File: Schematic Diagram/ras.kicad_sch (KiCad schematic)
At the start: 16 parts, among them Q1 S8050, SW2 SW_DPST_x2

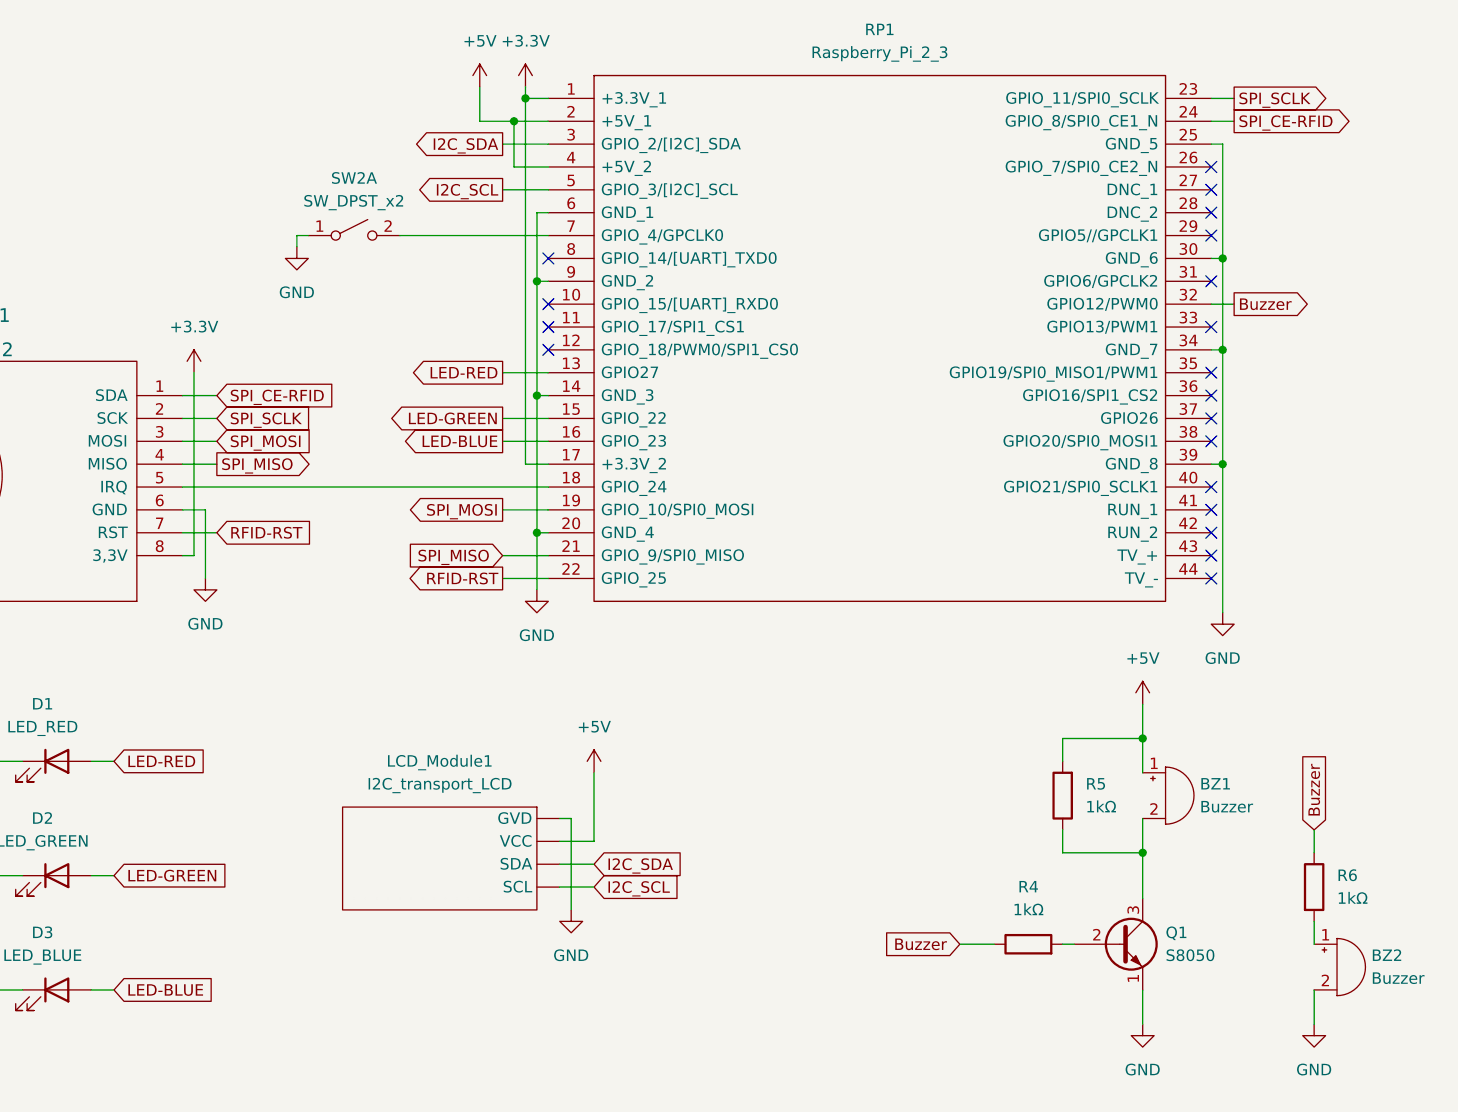
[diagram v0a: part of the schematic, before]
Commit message: update kicad before 9.0 after 8.0
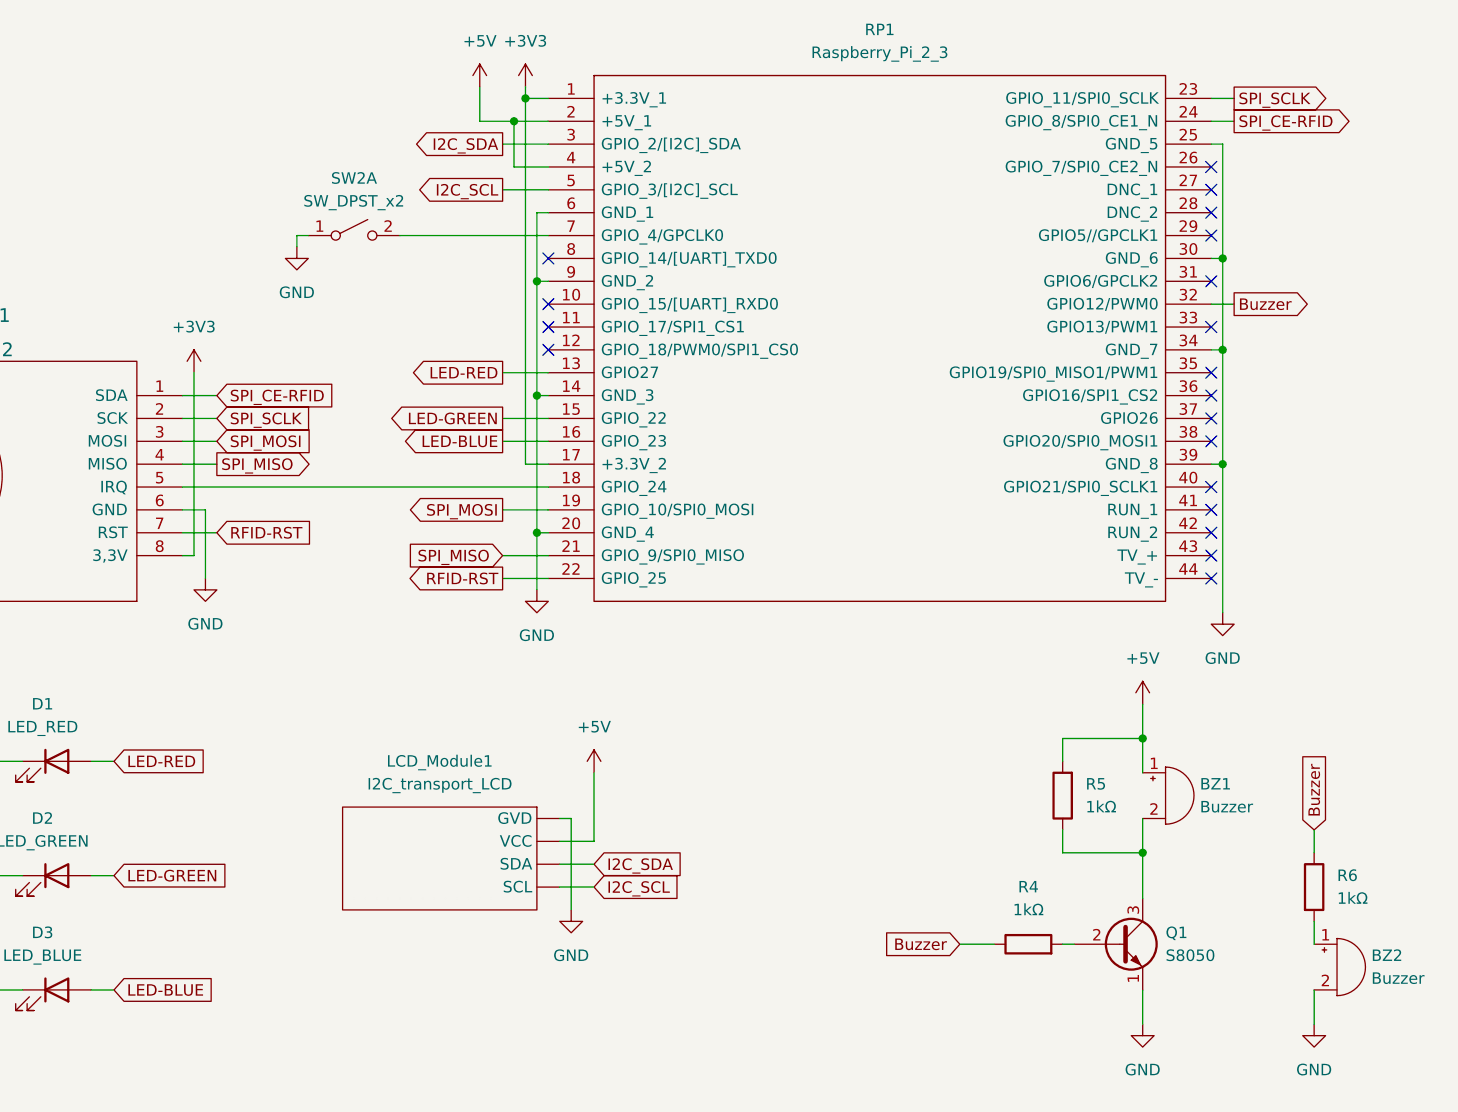
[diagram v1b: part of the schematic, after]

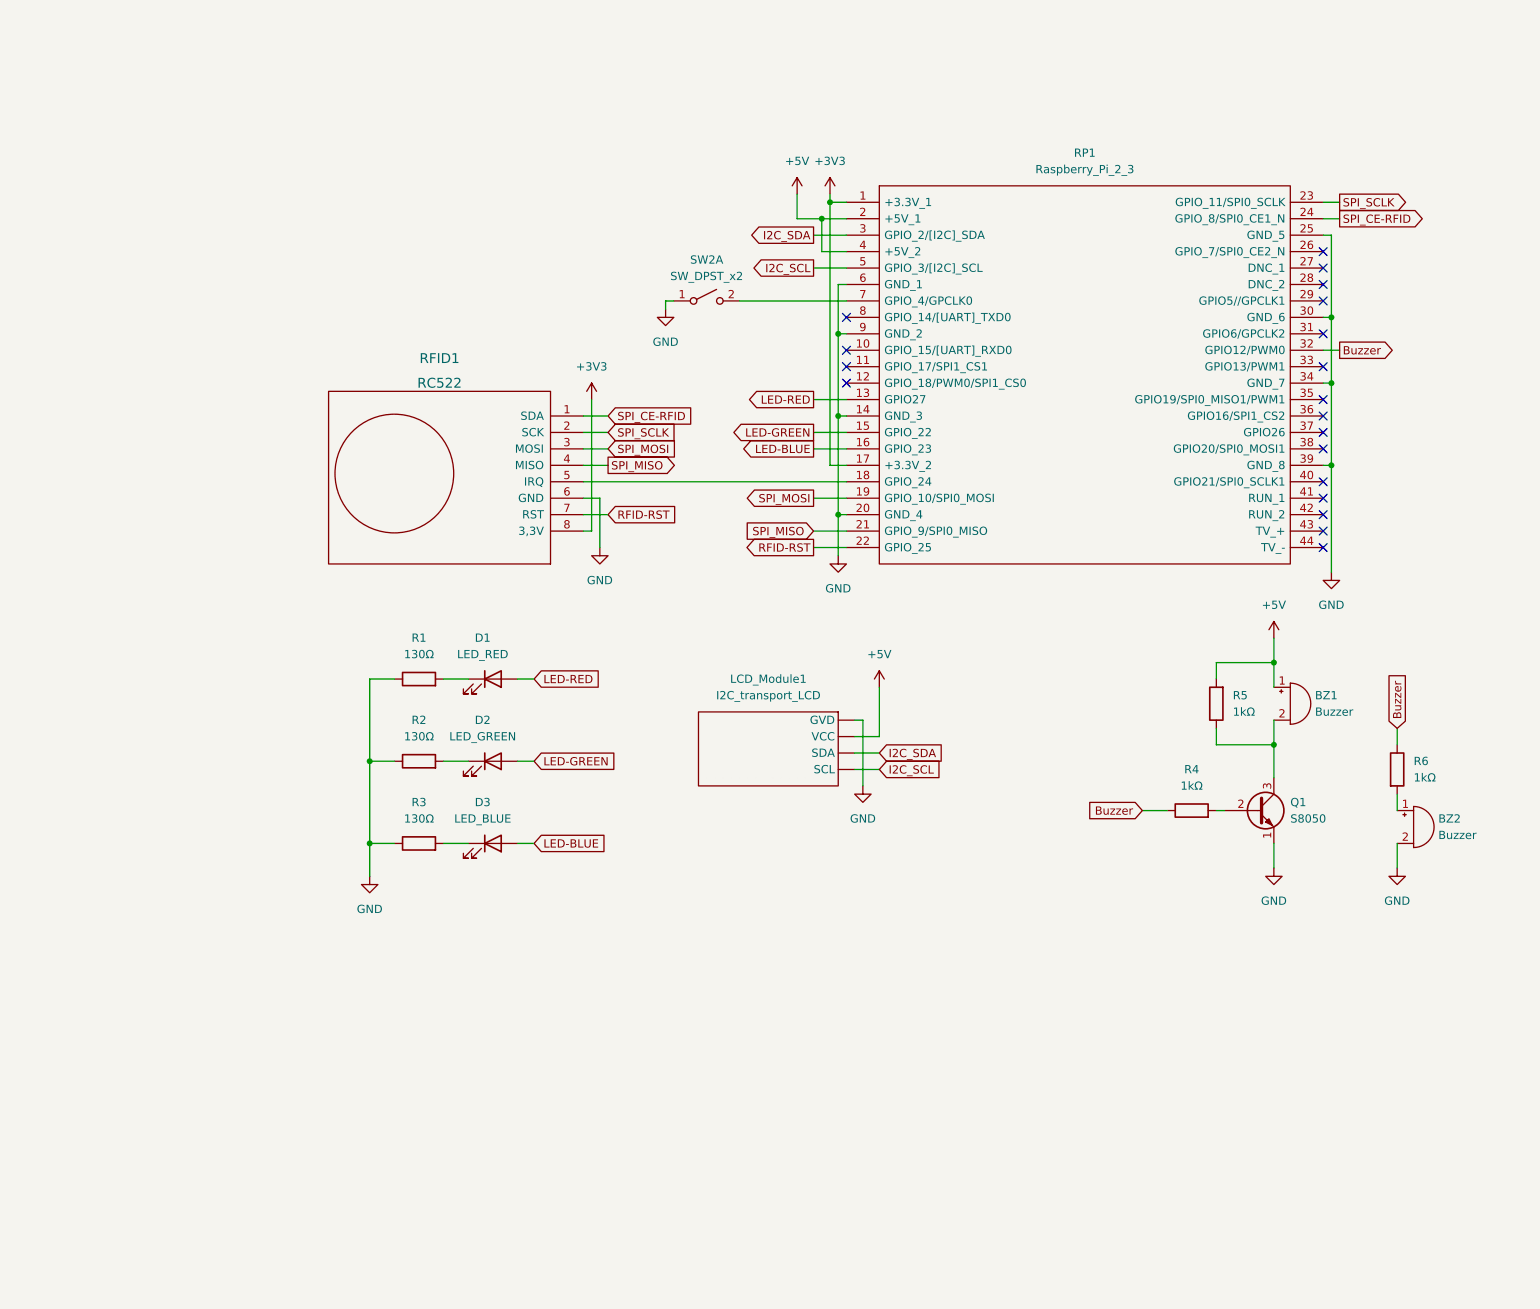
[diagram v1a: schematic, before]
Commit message: update ras and vertify RFID and LED
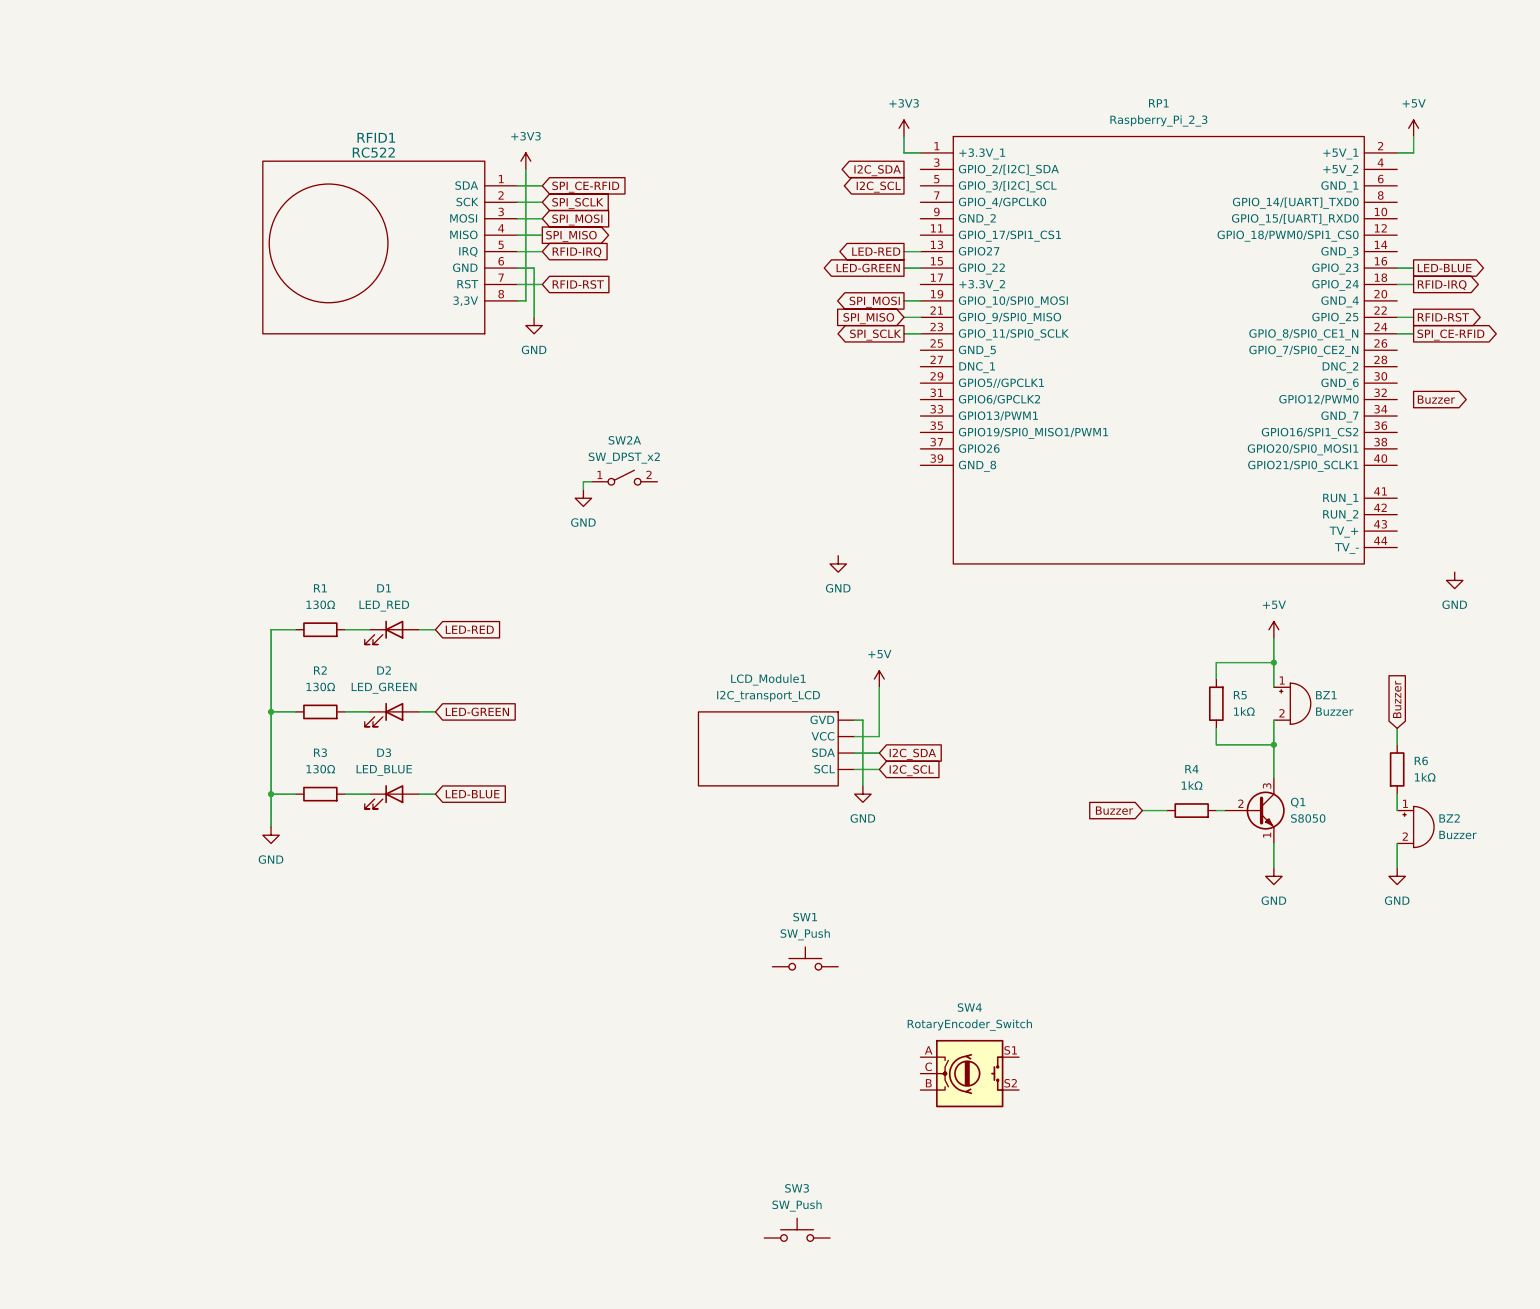
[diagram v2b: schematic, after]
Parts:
- added SW1, SW3: SW_Push, symbol Switch:SW_Push
- added SW4: RotaryEncoder_Switch, symbol Device:RotaryEncoder_Switch
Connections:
- net +3V3: no longer RP1.17 (+3.3V_2)
- net +5V: no longer RP1.4 (+5V_2)
- net Buzzer: no longer RP1.32 (GPIO12/PWM0)
- net GND: no longer RP1.14 (GND_3), RP1.20 (GND_4), RP1.25 (GND_5), RP1.30 (GND_6), RP1.34 (GND_7), RP1.39 (GND_8), RP1.6 (GND_1), RP1.9 (GND_2)
- net I2C_SCL: no longer RP1.5 (GPIO_3/[I2C]_SCL)
- net I2C_SDA: no longer RP1.3 (GPIO_2/[I2C]_SDA)
- net at SW2.2 (B): no longer RP1.7 (GPIO_4/GPCLK0)
- net RFID-IRQ: now reaches RFID1.5 (IRQ), RP1.18 (GPIO_24)
- no-connect marks 19 -> 0
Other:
- moved on the sheet: D1, D2, D3, R1, R2, R3, RFID1, RP1, SW2A

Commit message: verify I2C
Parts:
- added U2: ~, symbol project:AT24C32
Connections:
- net +5V: now also U2.5 (VCC)
- net GND: now also U2.6 (GND)
- net I2C_SCL: now also RP1.5 (GPIO_3/[I2C]_SCL), U2.3 (SCL)
- net I2C_SDA: now also RP1.3 (GPIO_2/[I2C]_SDA), U2.4 (SDA)
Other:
- moved on the sheet: LCD_Module1

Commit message: vertify encoder and button
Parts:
- removed SW2: SW_DPST_x2, symbol Switch:SW_DPST_x2
- removed SW3: SW_Push, symbol Switch:SW_Push
- added SW5, SW7, SW8, SW9: SW_Push, symbol Switch:SW_Push
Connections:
- net GND: now also SW1.1, SW4.C, SW4.S2, SW5.1, SW7.1, SW8.1, SW9.1
- net ENCODER_A: now reaches SW4.A
- net ENCODER_A: now also RP1.38 (GPIO20/SPI0_MOSI1)
- net ENCODER_B: now reaches SW4.B
- net ENCODER_B: now also RP1.40 (GPIO21/SPI0_SCLK1)
- net DONE_BUTTON: now reaches SW4.S1
- net DONE_BUTTON: now also RP1.35 (GPIO19/SPI0_MISO1/PWM1)
- net HOME_BUTTON: now reaches RP1.29 (GPIO5//GPCLK1)
- net HOME_BUTTON: now also SW7.2
- net MENU_BUTTON: now reaches RP1.31 (GPIO6/GPCLK2)
- net MENU_BUTTON: now also SW5.2
- net PREVIOUS_BUTTON: now reaches RP1.33 (GPIO13/PWM1)
- net PREVIOUS_BUTTON: now also SW8.2
- net NEXT_BUTTON: now reaches RP1.37 (GPIO26)
- net NEXT_BUTTON: now also SW9.2
- net SHUTDOWN_BUTTON: now reaches RP1.7 (GPIO_4/GPCLK0)
- net SHUTDOWN_BUTTON: now also SW1.2
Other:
- moved on the sheet: SW1, SW4

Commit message: check ERC
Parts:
- renumbered SW7 to SW2, SW5 to SW3, SW8 to SW4, SW4 to SW5, SW9 to SW6, U2 to U1
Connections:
- net +5V: now also LCD_Module1.2 (VCC); no longer LCD_Module1. (SCL)
- net Buzzer: now also RP1.32 (GPIO12/PWM0)
- net GND: now also LCD_Module1.1 (GND), RP1.14 (GND_3), RP1.20 (GND_4), RP1.25 (GND_5), RP1.30 (GND_6), RP1.34 (GND_7), RP1.39 (GND_8), RP1.6 (GND_1), RP1.9 (GND_2); no longer LCD_Module1. (SCL)
- net I2C_SCL: now also LCD_Module1.4 (SCL); no longer LCD_Module1. (SCL)
- net I2C_SDA: now also LCD_Module1.3 (SDA); no longer LCD_Module1. (SCL)
- no-connect marks 0 -> 16
